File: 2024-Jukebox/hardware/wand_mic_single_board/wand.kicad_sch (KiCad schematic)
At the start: 48 parts, among them J1 USB_C_Receptacle_USB2.0, J2 Conn_01x05, J3 Conn_01x04, J4 Conn_01x04, J5 Conn_01x04, J6 Conn_01x01, J7 Conn_01x04, Q1 MUN5214DW1T1G, Q2 BSS138, Q3 CJ3139K, Q5 BSS138, SW1 SW_SPDT, U1 CP2104, U2 ESP32-PICO-D4, U3 ICM-20948, U4 TP4065-4.2V, U5 NCP167BMX330TBG, U6 LY68L6400SLIT, U7 MIC5225-1.8

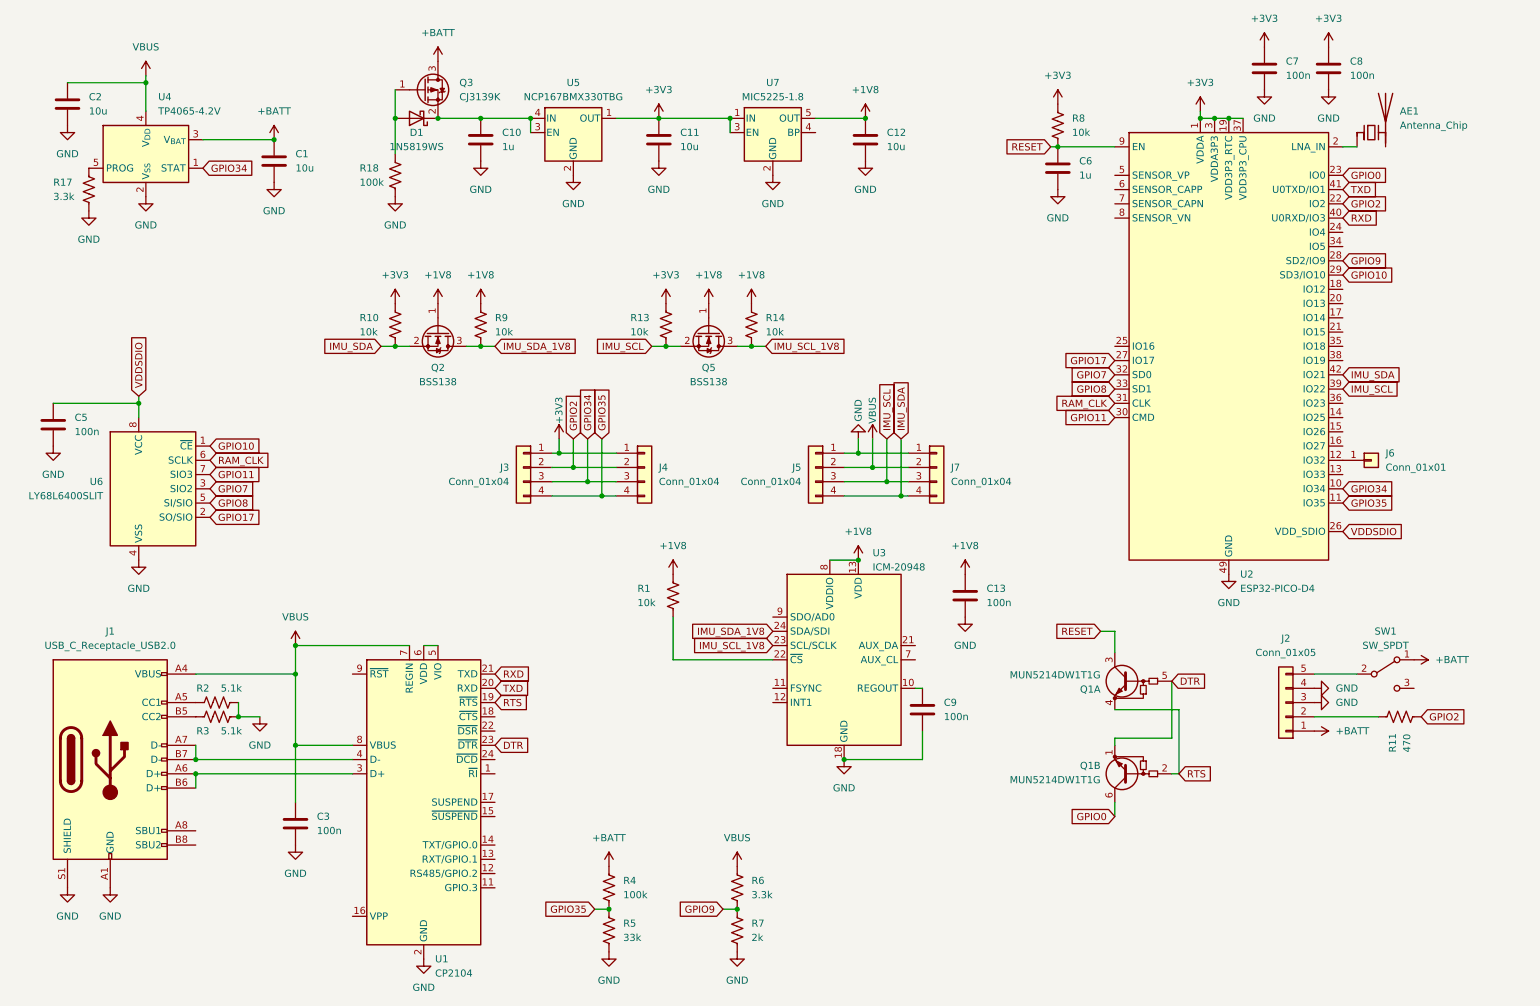
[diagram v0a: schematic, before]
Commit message: Added single board wand design
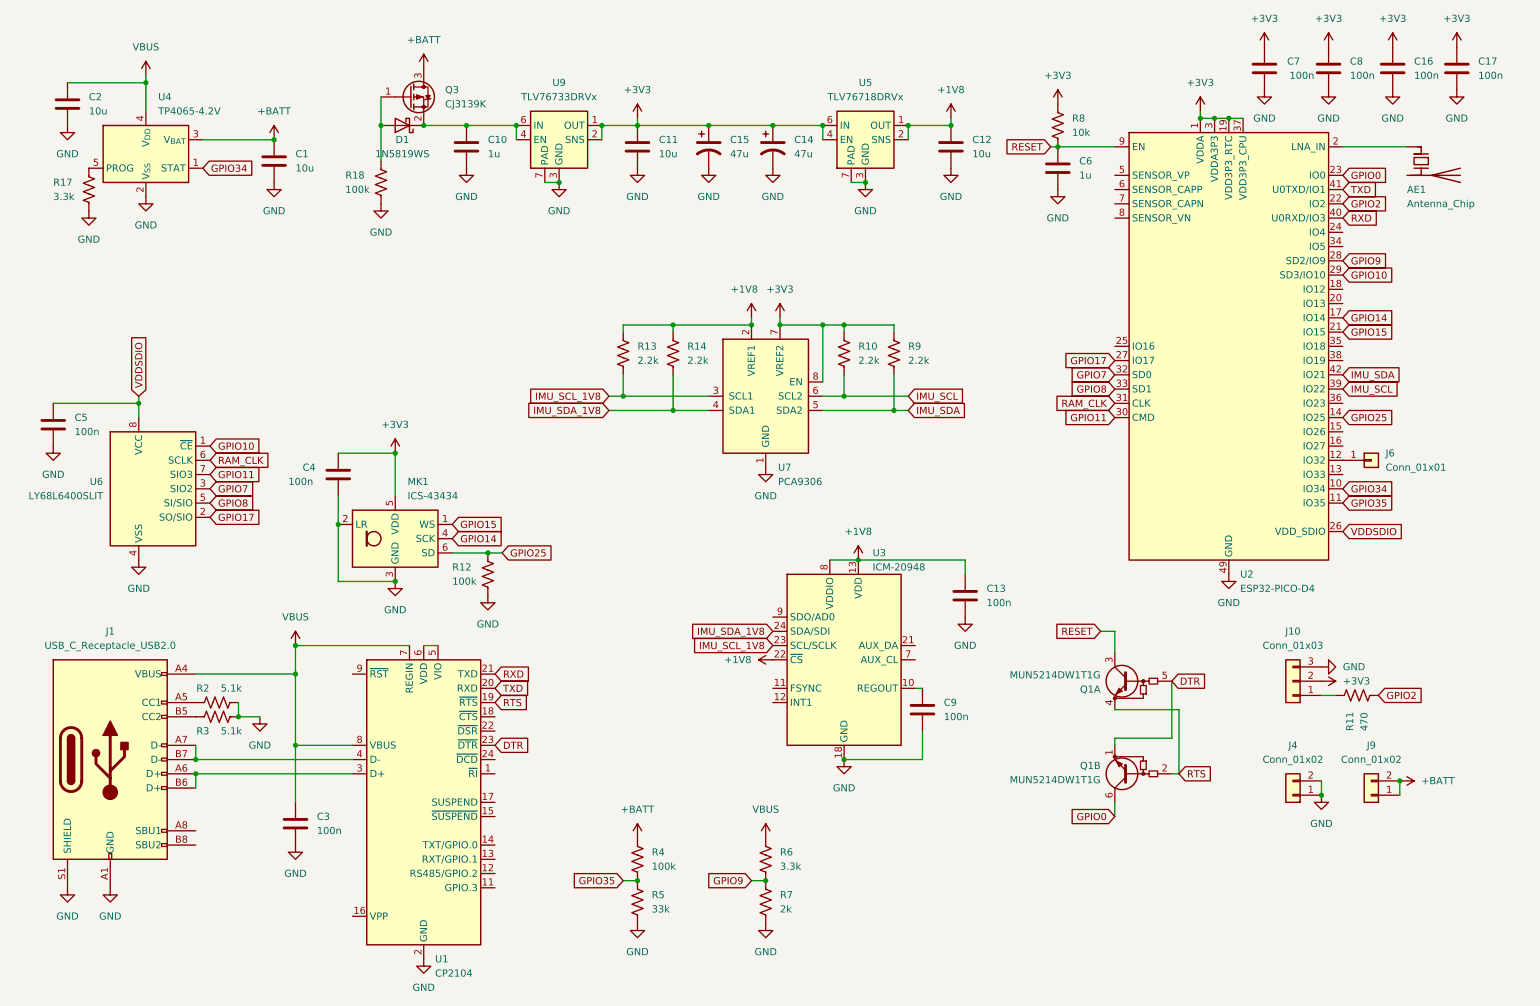
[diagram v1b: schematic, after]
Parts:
- removed J2: Conn_01x05, Connector_PinHeader_2.54mm:PinHeader_1x05_P2.54mm_Vertical, symbol Connector_Generic:Conn_01x05
- removed J3, J4, J5, J7: Conn_01x04, Connector_PinHeader_2.54mm:PinHeader_1x04_P2.54mm_Vertical, symbol Connector_Generic:Conn_01x04
- removed Q2, Q5: BSS138, Package_TO_SOT_SMD:SOT-23, symbol Transistor_FET:BSS138
- removed R1: 10k, Resistor_SMD:R_0402_1005Metric, symbol Device:R_US
- removed SW1: SW_SPDT, Button_Switch_THT:SW_CuK_OS102011MA1QN1_SPDT_Angled, symbol Switch:SW_SPDT
- removed U5: NCP167BMX330TBG, Package_DFN_QFN:OnSemi_XDFN4-1EP_1.0x1.0mm_EP0.52x0.52mm, symbol Regulator_Linear:MIC5205-2.5YM5
- removed U7: MIC5225-1.8, Package_TO_SOT_SMD:SOT-23-5, symbol Regulator_Linear:MIC5205-2.5YM5
- added C14, C15: 47u, Capacitor_SMD:C_0805_2012Metric, symbol Device:C_Polarized_US
- added C16, C17, C4: 100n, Capacitor_SMD:C_0402_1005Metric, symbol Device:C
- added J10: Conn_01x03, Connector_PinHeader_2.54mm:PinHeader_1x03_P2.54mm_Vertical, symbol Connector_Generic:Conn_01x03
- added J4, J9: Conn_01x02, Connector_PinHeader_2.54mm:PinHeader_1x02_P2.54mm_Vertical, symbol Connector_Generic:Conn_01x02
- added MK1: ICS-43434, Sensor_Audio:InvenSense_ICS-43434-6_3.5x2.65mm, symbol Sensor_Audio:ICS-43434
- added R12: 100k, Resistor_SMD:R_0402_1005Metric, symbol Device:R_US
- added U5: TLV76718DRVx, Package_SON:WSON-6-1EP_2x2mm_P0.65mm_EP1x1.6mm_ThermalVias, symbol Regulator_Linear:TLV76718DRVx
- added U7: PCA9306, Package_SO:VSSOP-8_2.3x2mm_P0.5mm, symbol Interface:PCA9306
- added U9: TLV76733DRVx, Package_SON:WSON-6-1EP_2x2mm_P0.65mm_EP1x1.6mm_ThermalVias, symbol Regulator_Linear:TLV76733DRVx
- AE1: footprint Capacitor_SMD:C_1206_3216Metric -> AlexCustom:NN01-102
- R10, R13, R14, R9: value 10k -> 2.2k
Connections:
- net +1V8: now also R13.1, U3.22 (~{CS}), U5.1 (OUT), U5.2 (SNS), U7.2 (VREF1); no longer R9.1
- net +3V3: now also R9.1, C14.1, C15.1, C16.1, C17.1, C4.1, J10.2 (Pin_2), MK1.5 (VDD), U5.4 (EN), U5.6 (IN), U7.7 (VREF2), U7.8 (EN), U9.1 (OUT), U9.2 (SNS); no longer R13.1
- net +BATT: now also J9.1 (Pin_1), J9.2 (Pin_2)
- net GND: now also C14.2, C15.2, C16.2, C17.2, C4.2, J10.3 (Pin_3), J4.1 (Pin_1), J4.2 (Pin_2), MK1.2 (LR), MK1.3 (GND), R12.2, U5.3 (GND), U5.5 (GND), U5.7 (PAD), U7.1 (GND), U9.3 (GND), U9.5 (GND), U9.7 (PAD)
- net IMU_SCL: now also R10.2, U7.6 (SCL2); no longer R13.2
- net IMU_SCL_1V8: now also R13.2, U7.3 (SCL1); no longer R14.2
- net IMU_SDA: now also R9.2, U7.5 (SDA2); no longer R10.2
- net IMU_SDA_1V8: now also R14.2, U7.4 (SDA1); no longer R9.2
- net GPIO25: now reaches U2.14 (IO25)
- net GPIO25: now also MK1.6 (SD), R12.1
- net GPIO14: now reaches U2.17 (IO14)
- net GPIO14: now also MK1.4 (SCK)
- net GPIO15: now reaches U2.21 (IO15)
- net GPIO15: now also MK1.1 (WS)
- net at C10.1, D1.1 (K), Q3.2 (S): now also U9.4 (EN), U9.6 (IN)
- net at R11.1: now also J10.1 (Pin_1)
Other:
- moved on the sheet: AE1, C10, C11, C12, D1, Q3, R11, R18, R4, R5, R6, R7

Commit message: Updated wand PCBs
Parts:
- removed C14, C15: 47u, Capacitor_SMD:C_0805_2012Metric, symbol Device:C_Polarized_US
- added C22, C23, C24, C25: 10u, Capacitor_SMD:C_0402_1005Metric, symbol Device:C
- C9: footprint Capacitor_SMD:C_0402_1005Metric -> Capacitor_SMD:C_0603_1608Metric
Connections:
- net +3V3: now also C22.1, C23.1, C24.1, C25.1
- net GND: now also C22.2, C23.2, C24.2, C25.2
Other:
- moved on the sheet: AE1, C11, C12, C13, C16, C17, C6, C7, C8, C9, J10, J4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
